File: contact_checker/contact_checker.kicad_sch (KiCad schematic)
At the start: 39 parts, among them J1 DB9_Female_MountingHoles, J10 Conn_01x01_Female, J11 Conn_01x01_Female, J12 Conn_01x01_Female, J13 Conn_Triaxial, J14 Conn_Triaxial, J15 Conn_Triaxial, J16 Conn_Triaxial, J17 Conn_01x01_Female, J18 Conn_01x01_Female, J19 Conn_Triaxial, J2 Conn_01x08, J20 Conn_01x01_Female, J21 Conn_01x01_Female, J22 Conn_01x01_Female, J23 Conn_01x01_Female, J24 Conn_01x01_Female, J25 Conn_Triaxial, J26 RJ45_Shielded, J27 RJ45_Shielded, J28 Conn_01x08, J29 Conn_01x08, J3 DB9_Male_MountingHoles, J30 Conn_01x03, J31 Conn_02x03_Odd_Even, J32 Conn_02x03_Odd_Even, J33 Conn_01x04, J4 Conn_Triaxial, J5 Conn_01x01_Female, J6 Conn_01x01_Female, J7 Conn_Triaxial, J8 Conn_01x01_Female, J9 Conn_01x01_Female, K1 EC2-5NU, K2 EC2-5NU

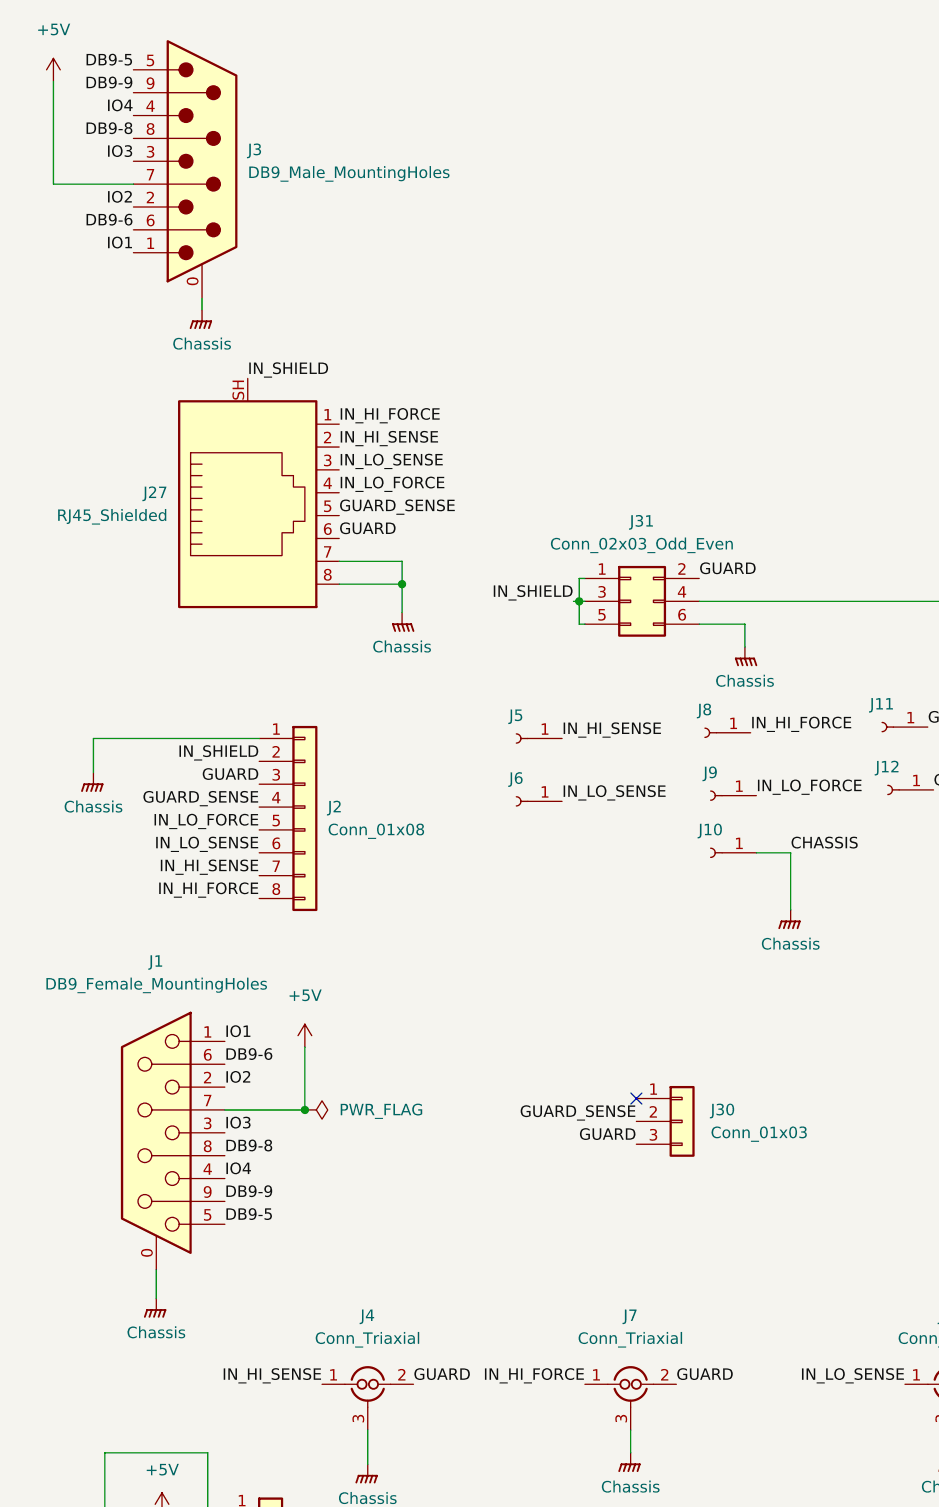
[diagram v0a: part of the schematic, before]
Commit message: switch to stacked DB9 connector to save edge space
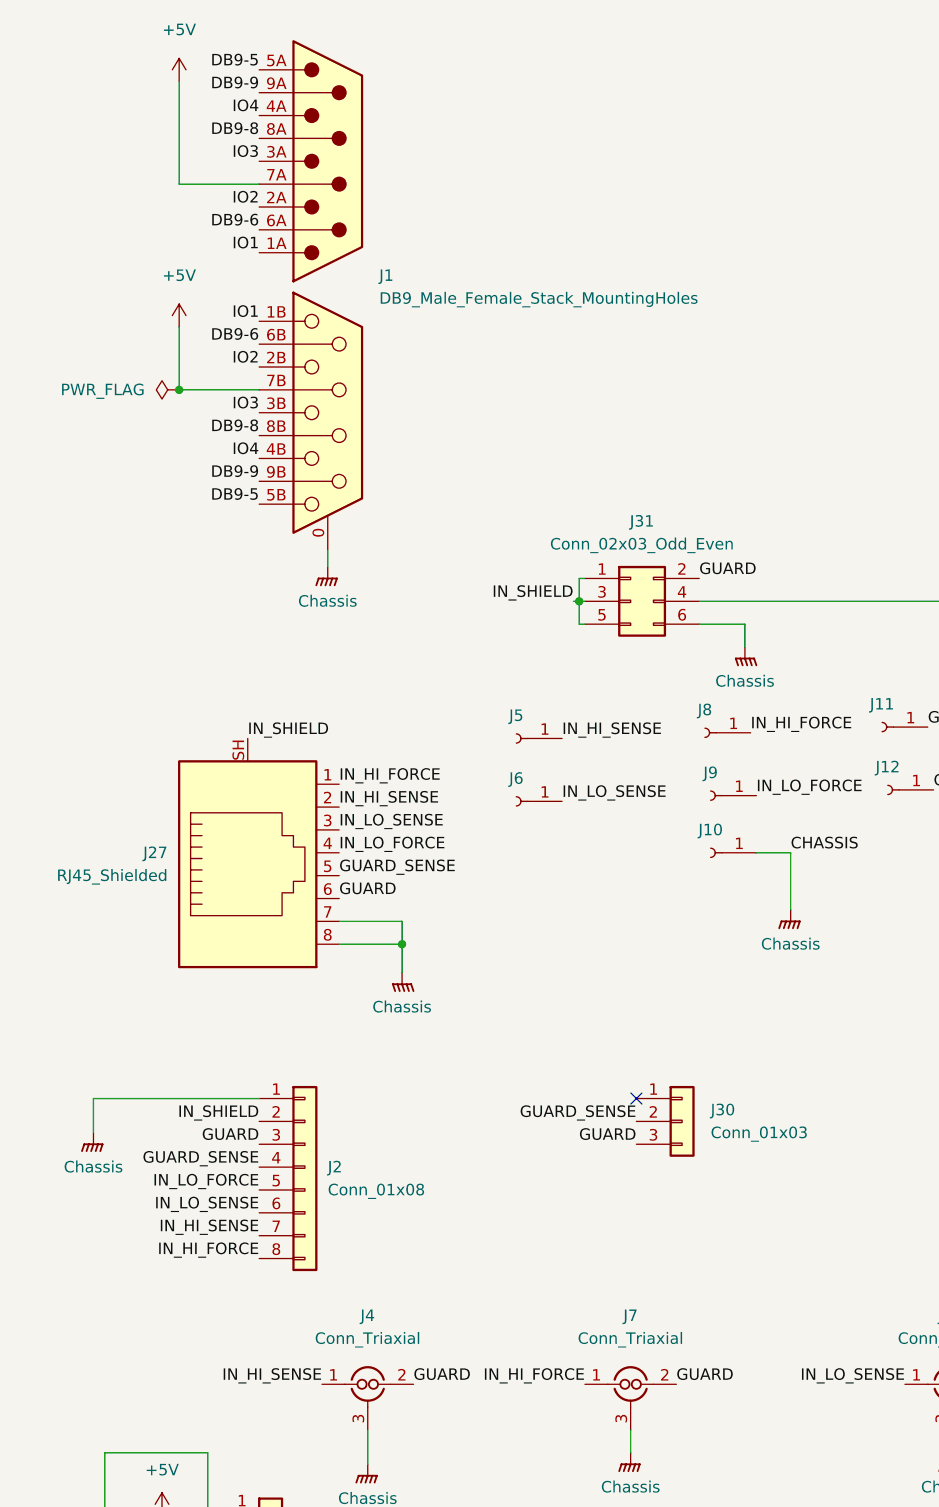
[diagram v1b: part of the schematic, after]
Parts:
- removed J1: DB9_Female_MountingHoles, Connector_Dsub:DSUB-9_Female_Vertical_P2.77x2.84mm_MountingHoles, symbol Connector:DB9_Female_MountingHoles
- removed J3: DB9_Male_MountingHoles, Connector_Dsub:DSUB-9_Male_Vertical_P2.77x2.84mm_MountingHoles, symbol Connector:DB9_Male_MountingHoles
- added J1: DB9_Male_Female_Stack_MountingHoles, custom_footprints:DSUB-9_Male_Female_Vertical_Stack_P2.77x2.84mm_MountingHoles, symbol cusom_symbols:DB9_Male_Female_Stack_MountingHoles
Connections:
- net +5V: now also J1.7A, J1.7B
- net DB9-5: now also J1.5A, J1.5B
- net DB9-6: now also J1.6A, J1.6B
- net DB9-8: now also J1.8A, J1.8B
- net DB9-9: now also J1.9A, J1.9B
- net GNDPWR: now also J1.0 (PAD)
- net IO1: now also J1.1A, J1.1B
- net IO2: now also J1.2A, J1.2B
- net IO3: now also J1.3A, J1.3B
- net IO4: now also J1.4A, J1.4B
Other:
- moved on the sheet: J2, J27

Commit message: rev3 on contact checker boards
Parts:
- removed J2, J29: Conn_01x08, Connector_PinHeader_2.54mm:PinHeader_1x08_P2.54mm_Horizontal, symbol Connector_Generic:Conn_01x08
- removed J33: Conn_01x04, Connector_PinHeader_2.54mm:PinHeader_1x04_P2.54mm_Horizontal, symbol Connector_Generic:Conn_01x04
- added J2: Conn_02x06_Odd_Even, Connector_PinHeader_2.54mm:PinHeader_2x06_P2.54mm_Horizontal, symbol Connector_Generic:Conn_02x06_Odd_Even
- added J29: Conn_02x04_Odd_Even, Connector_PinHeader_2.54mm:PinHeader_2x04_P2.54mm_Horizontal, symbol Connector_Generic:Conn_02x04_Odd_Even
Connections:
- net +5V: now also J2.12 (Pin_12)
- net GNDPWR: now also J2.10 (Pin_10), J2.8 (Pin_8), J29.2 (Pin_2); no longer J28.7 (Pin_7)
- net GUARD: now also J2.4 (Pin_4), J29.6 (Pin_6)
- net GUARD_SENSE: now also J2.2 (Pin_2), J29.8 (Pin_8)
- net IN_HI_FORCE: now also J2.1 (Pin_1)
- net IN_HI_SENSE: now also J2.3 (Pin_3)
- net IN_LO_FORCE: now also J2.7 (Pin_7)
- net IN_LO_SENSE: now also J2.5 (Pin_5)
- net IN_SHIELD: now also J2.6 (Pin_6)
- net IO1: now also J2.11 (Pin_11)
- net IO2: now also J2.9 (Pin_9)
- net OUT_HI_FORCE: now also J29.7 (Pin_7)
- net OUT_HI_SENSE: now also J29.5 (Pin_5)
- net OUT_LO_FORCE: now also J29.1 (Pin_1)
- net OUT_LO_SENSE: now also J29.3 (Pin_3)
- net OUT_SHIELD: now also J28.7 (Pin_7), J29.4 (Pin_4)
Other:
- moved on the sheet: J28

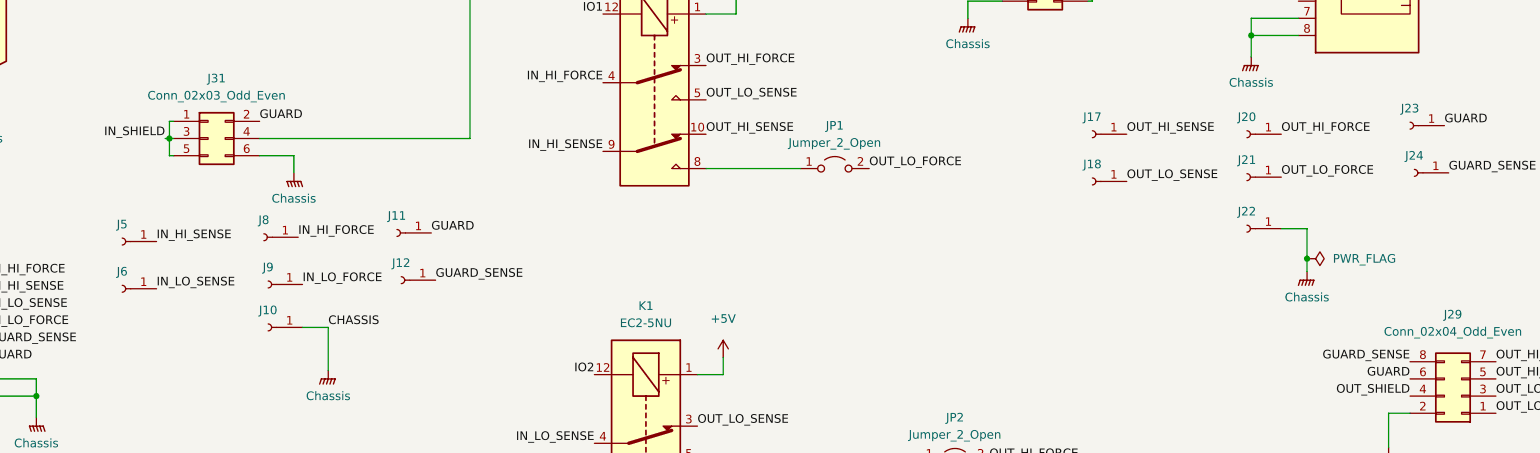
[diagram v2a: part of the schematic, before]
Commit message: new holder pcbs
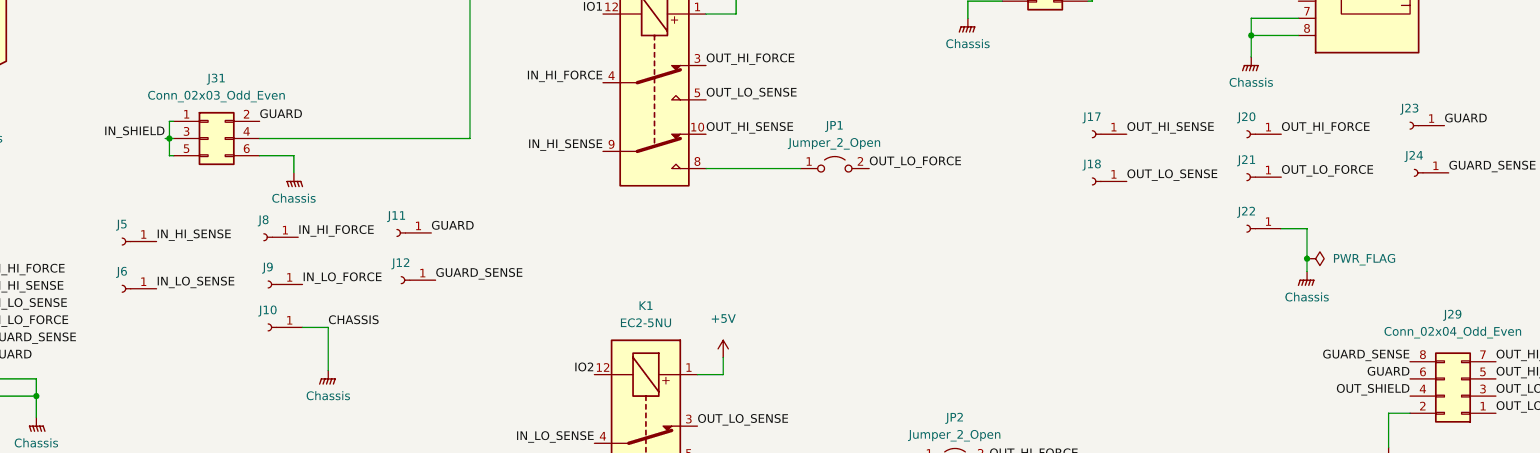
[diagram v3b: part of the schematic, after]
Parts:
- K1, K2: footprint Relay_THT:Relay_DPDT_Kemet_EC2 -> custom_footprints:Relay_DPDT_Kemet_EC2

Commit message: change some logos
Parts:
- LOGO1, LOGO2: footprint custom_footprints:logo -> custom_footprints:logo_small
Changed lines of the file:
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@@
       (effects (font (size 1.27 1.27)) hide)
     )
-    (property "Footprint" "custom_footprints:logo" (at 184.785 174.625 0)
+    (property "Footprint" "custom_footprints:logo_small" (at 184.785 174.625 0)
       (effects (font (size 1.27 1.27)) hide)
     )
@@
       (effects (font (size 1.27 1.27)) hide)
     )
-    (property "Footprint" "custom_footprints:logo" (at 276.86 174.625 0)
-      (effects (font (size 1.27 1.27)) hide)
-    )
+    (property "Footprint" "custom_footprints:logo_small" (at 276.86 174.625 0)
+      (effects (font (size 1.27 1.27)) hide)
+    )

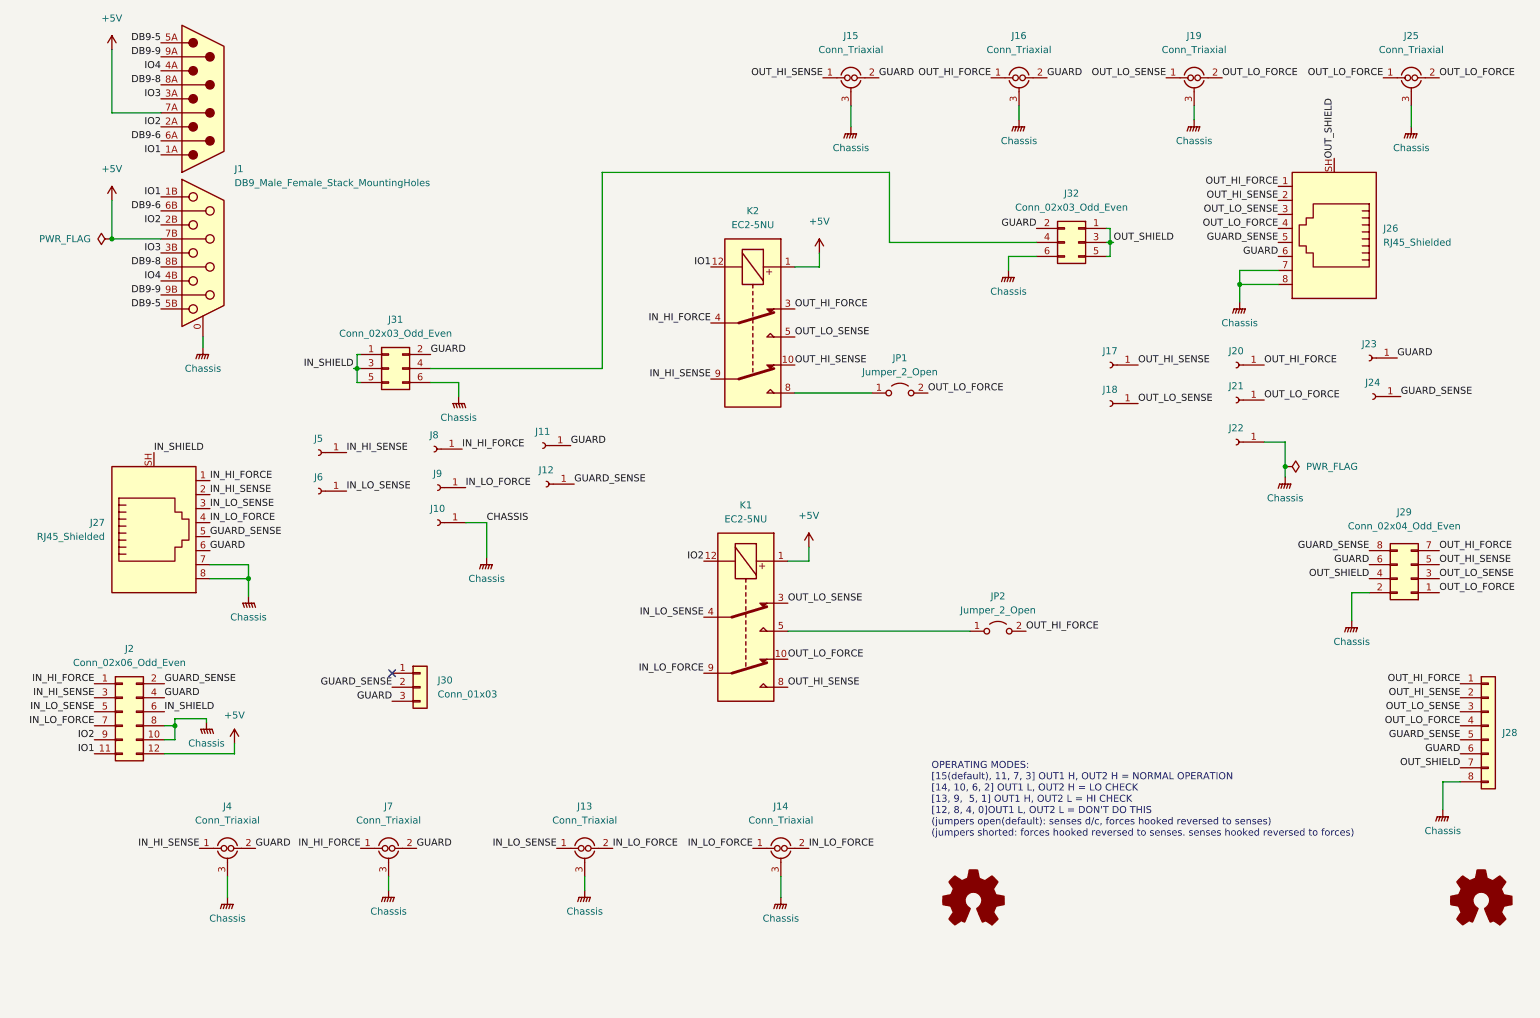
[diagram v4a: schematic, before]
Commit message: upgrade contact checker with sense circuitry
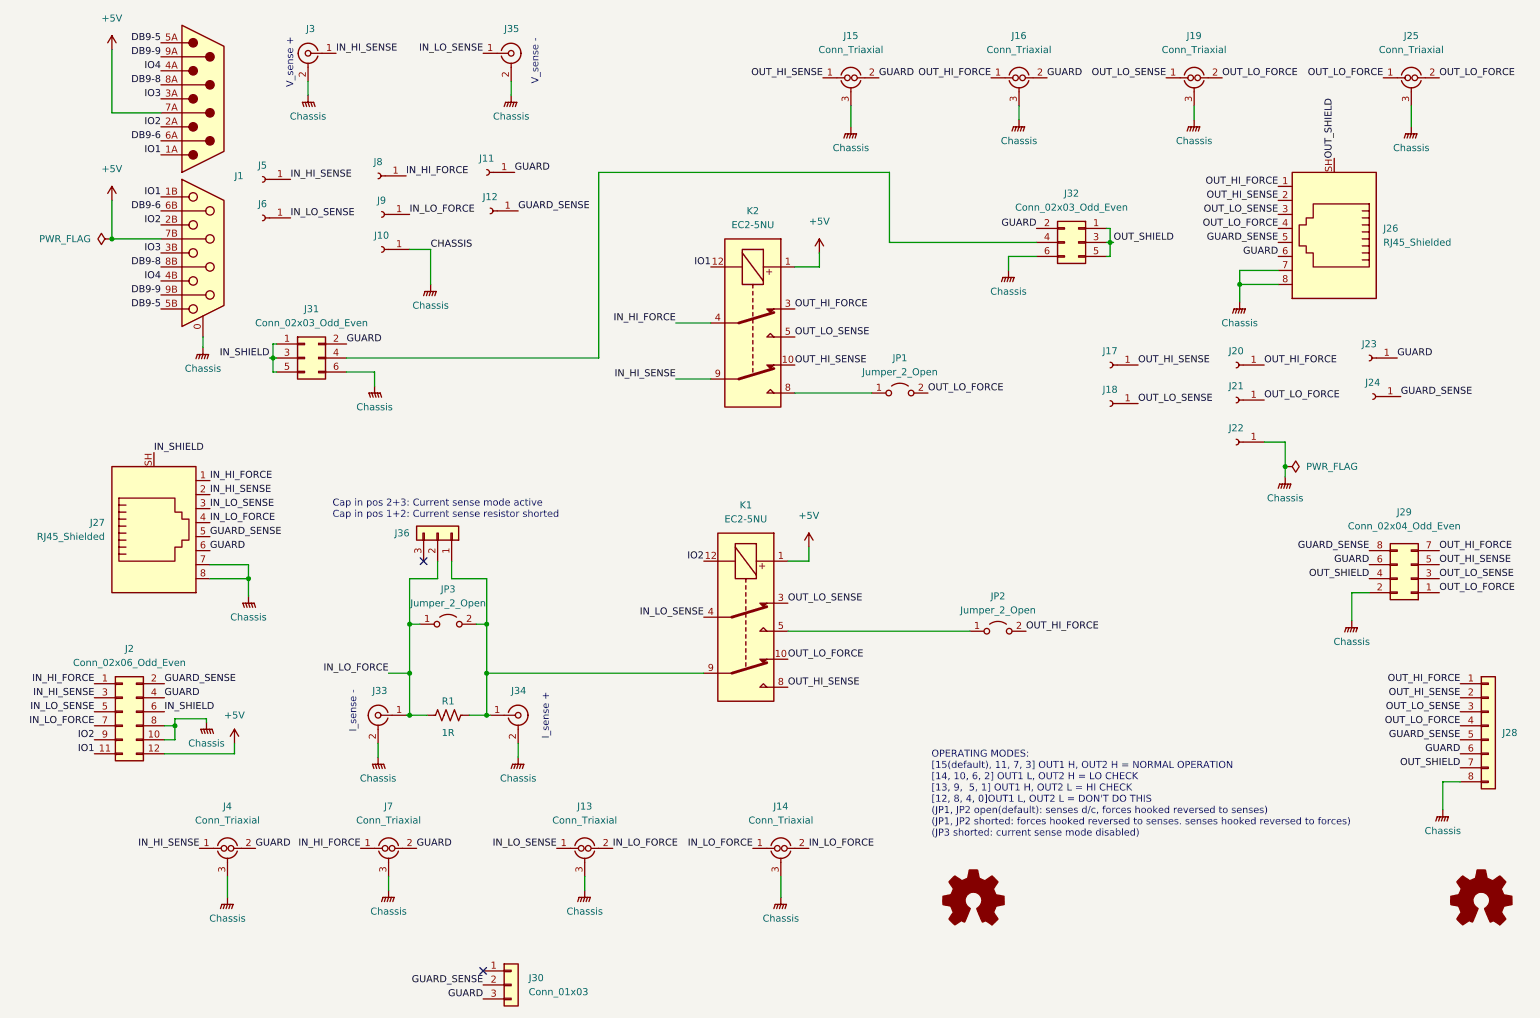
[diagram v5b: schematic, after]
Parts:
- added J3, J33, J34, J35: Conn_Coaxial, Connector_Coaxial:U.FL_Molex_MCRF_73412-0110_Vertical, symbol Connector:Conn_Coaxial
- added J36: Conn_01x03, Connector_PinHeader_2.54mm:PinHeader_1x03_P2.54mm_Horizontal, symbol Connector_Generic:Conn_01x03
- added JP3: Jumper_2_Open, Jumper:SolderJumper-2_P1.3mm_Open_RoundedPad1.0x1.5mm, symbol Jumper:Jumper_2_Open
- added R1: 1R, Resistor_SMD:R_2512_6332Metric_Pad1.40x3.35mm_HandSolder, symbol Device:R_US
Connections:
- net GNDPWR: now also J3.2 (Ext), J33.2 (Ext), J34.2 (Ext), J35.2 (Ext)
- net IN_HI_SENSE: now also J3.1 (In)
- net IN_LO_FORCE: now also J33.1 (In), J36.2 (Pin_2), JP3.1 (A), R1.1; no longer K1.9
- net IN_LO_SENSE: now also J35.1 (In)
- new net: J34.1 (In), J36.1 (Pin_1), JP3.2 (B), K1.9, R1.2
- no-connect marks 1 -> 2
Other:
- note added: "Cap in pos 2+3: Current sense mode active Cap in pos 1+2: Current sense resistor shorted"
- note added: "I_sense +"
- note added: "I_sense -"
- note added: "OPERATING MODES: [15(default), 11, 7, 3] OUT1 H, OUT2 H = NORMAL OPERATION [14, 10, 6, 2] OUT1 L, OUT2 H = LO CHECK [13, 9, 5, 1] OUT1 H, OUT2 L = HI CHECK [12, 8, 4, 0]OUT1 L, OUT2 L = DON'T DO THIS (JP1, JP2 open(default): senses d/c, forces hooked reversed to senses) (JP1, JP2 shorted: forces hooked reversed to senses. senses hooked reversed to forces) (JP3 shorted: current sense mode disabled)"
- note added: "V_sense +"
- note added: "V_sense -"
- note removed: "OPERATING MODES: [15(default), 11, 7, 3] OUT1 H, OUT2 H = NORMAL OPERATION [14, 10, 6, 2] OUT1 L, OUT2 H = LO CHECK [13, 9, 5, 1] OUT1 H, OUT2 L = HI CHECK [12, 8, 4, 0]OUT1 L, OUT2 L = DON'T DO THIS (jumpers open(default): senses d/c, forces hooked reversed to senses) (jumpers shorted: forces hooked reversed to senses. senses hooked reversed to forces)"
- moved on the sheet: J10, J11, J12, J30, J31, J5, J6, J8, J9

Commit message: add some missing copper
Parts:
- LOGO1, LOGO2: footprint custom_footprints:logo_small -> custom_footprints:logo
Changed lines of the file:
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@@
       (effects (font (size 1.27 1.27)) hide)
     )
-    (property "Footprint" "custom_footprints:logo_small" (at 184.785 174.625 0)
+    (property "Footprint" "custom_footprints:logo" (at 184.785 174.625 0)
       (effects (font (size 1.27 1.27)) hide)
     )
@@
       (effects (font (size 1.27 1.27)) hide)
     )
-    (property "Footprint" "custom_footprints:logo_small" (at 276.86 174.625 0)
-      (effects (font (size 1.27 1.27)) hide)
-    )
+    (property "Footprint" "custom_footprints:logo" (at 276.86 174.625 0)
+      (effects (font (size 1.27 1.27)) hide)
+    )

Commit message: contact checker fixups
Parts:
- added R2, R3, R4, R5: 5R, Resistor_SMD:R_2512_6332Metric_Pad1.40x3.35mm_HandSolder, symbol Device:R_US
- LOGO1, LOGO2: footprint custom_footprints:logo -> custom_footprints:site_small
- R1: value 1R -> 5R
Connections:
- net IN_LO_FORCE: now also R2.1, R3.1, R4.1, R5.1
- net at J34.1 (In), J36.1 (Pin_1), JP3.2 (B)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: now also R2.2, R3.2, R4.2, R5.2
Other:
- moved on the sheet: J4, J7

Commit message: fix up rj45 pad numbering
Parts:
- J2: footprint Connector_PinHeader_2.54mm:PinHeader_2x06_P2.54mm_Horizontal -> Connector_IDC:IDC-Header_2x06_P2.54mm_Horizontal
- J26, J27: footprint custom_footprints:RJ45_WURTH_615008142621_horizontal_shield -> custom_footprints:RJ45_WURTH_615008142621
- J29: footprint Connector_PinHeader_2.54mm:PinHeader_2x04_P2.54mm_Horizontal -> Connector_IDC:IDC-Header_2x04_P2.54mm_Horizontal
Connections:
- net GNDPWR: now also J26.1, J26.2, J27.1, J27.2; no longer J26.7, J26.8, J27.7, J27.8
- net GUARD: now also J26.3, J27.3; no longer J26.6, J27.6
- net GUARD_SENSE: now also J26.4, J27.4; no longer J26.5, J27.5
- net IN_HI_FORCE: now also J27.8; no longer J27.1
- net IN_HI_SENSE: now also J27.7; no longer J27.2
- net IN_LO_FORCE: now also J27.5; no longer J27.4
- net IN_LO_SENSE: now also J27.6; no longer J27.3
- net OUT_HI_FORCE: now also J26.8; no longer J26.1
- net OUT_HI_SENSE: now also J26.7; no longer J26.2
- net OUT_LO_FORCE: now also J26.5; no longer J26.4
- net OUT_LO_SENSE: now also J26.6; no longer J26.3
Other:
- moved on the sheet: J26, J27
